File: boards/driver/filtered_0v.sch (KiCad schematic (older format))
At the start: 3 parts

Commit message: Driver board: a bit more schematic work and some initial footprint selections
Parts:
- R228: footprint Resistor_SMD:R_1206_3216Metric -> Resistor_SMD:R_0603_1608Metric
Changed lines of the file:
@@
 F 0 "R229" V 4395 3600 50  0000 C CNN
 F 1 "3k" V 4486 3600 50  0000 C CNN
-F 2 "Resistor_SMD:R_1206_3216Metric" V 4640 3590 50  0001 C CNN
+F 2 "Resistor_SMD:R_0603_1608Metric" V 4640 3590 50  0001 C CNN
 F 3 "~" H 4600 3600 50  0001 C CNN
 	1    4600 3600

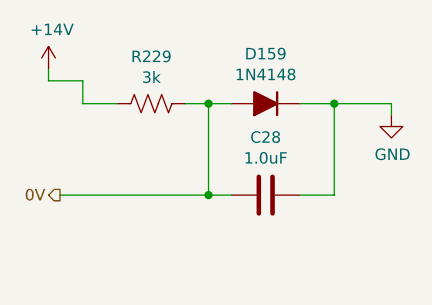
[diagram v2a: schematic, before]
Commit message: Driver board: fleshed out the hotswap controller, tweaked some resistors, and added some bypass caps
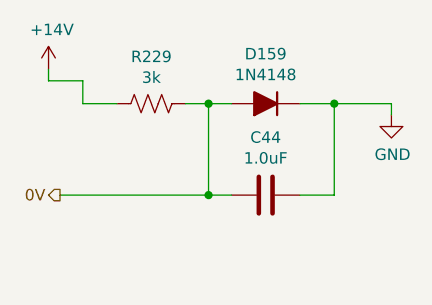
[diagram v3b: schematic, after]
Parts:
- renumbered C27 to C43
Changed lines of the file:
@@
 $EndDescr
 $Comp
-L lachesis:+14V #PWR0102
+L lachesis:+14V #PWR0105
 U 1 1 62980B09
 P 4150 3450
-AR Path="/6183FAE6/62980982/62980B09" Ref="#PWR0102"  Part="1"
-AR Path="/6183FAE6/6299B990/62980B09" Ref="#PWR0104"  Part="1"
-F 0 "#PWR0104" H 4150 3300 50  0001 C CNN
+AR Path="/6183FAE6/62980982/62980B09" Ref="#PWR0105"  Part="1"
+AR Path="/6183FAE6/6299B990/62980B09" Ref="#PWR0107"  Part="1"
+F 0 "#PWR0107" H 4150 3300 50  0001 C CNN
 F 1 "+14V" H 4165 3623 50  0000 C CNN
 F 2 "" H 4150 3450 50  0001 C CNN
@@
 0V
 $Comp
-L Device:C C27
+L Device:C C43
 U 1 1 62982B83
 P 5100 4000
-AR Path="/6183FAE6/62980982/62982B83" Ref="C27"  Part="1"
-AR Path="/6183FAE6/6299B990/62982B83" Ref="C28"  Part="1"
-F 0 "C28" V 4848 4000 50  0000 C CNN
+AR Path="/6183FAE6/62980982/62982B83" Ref="C43"  Part="1"
+AR Path="/6183FAE6/6299B990/62982B83" Ref="C44"  Part="1"
+F 0 "C44" V 4848 4000 50  0000 C CNN
 F 1 "1.0uF" V 4939 4000 50  0000 C CNN
 F 2 "" H 5138 3850 50  0001 C CNN
@@
 Connection ~ 5400 3600
 $Comp
-L power:GND #PWR0103
+L power:GND #PWR0106
 U 1 1 629836D4
 P 5650 3650
-AR Path="/6183FAE6/62980982/629836D4" Ref="#PWR0103"  Part="1"
-AR Path="/6183FAE6/6299B990/629836D4" Ref="#PWR0105"  Part="1"
-F 0 "#PWR0105" H 5650 3400 50  0001 C CNN
+AR Path="/6183FAE6/62980982/629836D4" Ref="#PWR0106"  Part="1"
+AR Path="/6183FAE6/6299B990/629836D4" Ref="#PWR0108"  Part="1"
+F 0 "#PWR0108" H 5650 3400 50  0001 C CNN
 F 1 "GND" H 5655 3477 50  0000 C CNN
 F 2 "" H 5650 3650 50  0001 C CNN

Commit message: Driver board: significant cleanup. Moved sense amp pairs into a subsheet, split tuning resistors into two globally, pushed input circuits into their corresponding sheets.
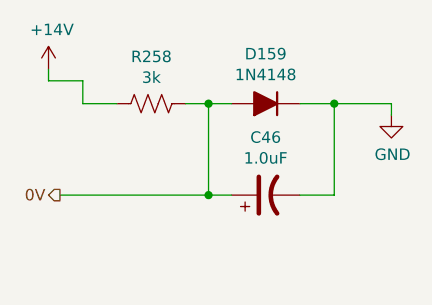
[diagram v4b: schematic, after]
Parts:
- removed C43: 1.0uF, symbol Device:C
- added C46: 1.0uF, Capacitor_Tantalum_SMD:CP_EIA-3216-18_Kemet-A, symbol Device:CP1
- renumbered R228 to R257
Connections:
- net 0V: now also C46.1
- net GND: now also C46.2
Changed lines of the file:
@@
 $Descr A4 11693 8268
 encoding utf-8
-Sheet 67 69
+Sheet 66 64
 Title ""
 Date ""
@@
 $EndDescr
 $Comp
-L lachesis:+14V #PWR0105
+L lachesis:+14V #PWR0122
 U 1 1 62980B09
 P 4150 3450
-AR Path="/6183FAE6/62980982/62980B09" Ref="#PWR0105"  Part="1"
-AR Path="/6183FAE6/6299B990/62980B09" Ref="#PWR0107"  Part="1"
-F 0 "#PWR0107" H 4150 3300 50  0001 C CNN
+AR Path="/6183FAE6/62980982/62980B09" Ref="#PWR0122"  Part="1"
+AR Path="/6183FAE6/6299B990/62980B09" Ref="#PWR0124"  Part="1"
+F 0 "#PWR0124" H 4150 3300 50  0001 C CNN
 F 1 "+14V" H 4165 3623 50  0000 C CNN
 F 2 "" H 4150 3450 50  0001 C CNN
@@
 $EndComp
 $Comp
-L Device:R_US R228
+L Device:R_US R257
 U 1 1 62981703
 P 4600 3600
-AR Path="/6183FAE6/62980982/62981703" Ref="R228"  Part="1"
-AR Path="/6183FAE6/6299B990/62981703" Ref="R229"  Part="1"
-F 0 "R229" V 4395 3600 50  0000 C CNN
+AR Path="/6183FAE6/62980982/62981703" Ref="R257"  Part="1"
+AR Path="/6183FAE6/6299B990/62981703" Ref="R258"  Part="1"
+F 0 "R258" V 4395 3600 50  0000 C CNN
 F 1 "3k" V 4486 3600 50  0000 C CNN
 F 2 "Resistor_SMD:R_0603_1608Metric" V 4640 3590 50  0001 C CNN
@@
 Text HLabel 4200 4000 0    50   Output ~ 0
 0V
-$Comp
-L Device:C C43
-U 1 1 62982B83
-P 5100 4000
-AR Path="/6183FAE6/62980982/62982B83" Ref="C43"  Part="1"
-AR Path="/6183FAE6/6299B990/62982B83" Ref="C44"  Part="1"
-F 0 "C44" V 4848 4000 50  0000 C CNN
-F 1 "1.0uF" V 4939 4000 50  0000 C CNN
-F 2 "" H 5138 3850 50  0001 C CNN
-F 3 "~" H 5100 4000 50  0001 C CNN
-	1    5100 4000
-	0    1    1    0
-$EndComp
 Wire Wire Line
 	4850 4000 4950 4000
@@
 Connection ~ 5400 3600
 $Comp
-L power:GND #PWR0106
+L power:GND #PWR0123
 U 1 1 629836D4
 P 5650 3650
-AR Path="/6183FAE6/62980982/629836D4" Ref="#PWR0106"  Part="1"
-AR Path="/6183FAE6/6299B990/629836D4" Ref="#PWR0108"  Part="1"
-F 0 "#PWR0108" H 5650 3400 50  0001 C CNN
+AR Path="/6183FAE6/62980982/629836D4" Ref="#PWR0123"  Part="1"
+AR Path="/6183FAE6/6299B990/629836D4" Ref="#PWR0125"  Part="1"
+F 0 "#PWR0125" H 5650 3400 50  0001 C CNN
 F 1 "GND" H 5655 3477 50  0000 C CNN
 F 2 "" H 5650 3650 50  0001 C CNN
@@
 	1    0    0    -1
 $EndComp
+$Comp
+L Device:CP1 C46
+U 1 1 628500B5
+P 5100 4000
+AR Path="/6183FAE6/6299B990/628500B5" Ref="C46"  Part="1"
+AR Path="/6183FAE6/62980982/628500B5" Ref="C45"  Part="1"
+F 0 "C46" V 5352 4000 50  0000 C CNN
+F 1 "1.0uF" V 5261 4000 50  0000 C CNN
+F 2 "Capacitor_Tantalum_SMD:CP_EIA-3216-18_Kemet-A" H 5100 4000 50  0001 C CNN
+F 3 "~" H 5100 4000 50  0001 C CNN
+	1    5100 4000
+	0    -1   -1   0
+$EndComp
 $EndSCHEMATC

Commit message: Driver board: integrated DIN 41612 backplane connector, and made a dedicated parity inhibit sheet with a different set resistor value.
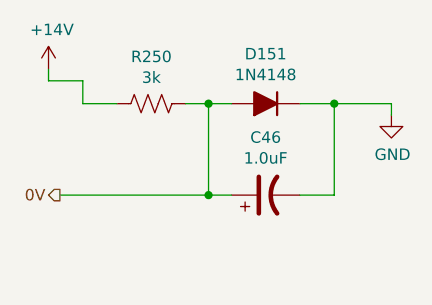
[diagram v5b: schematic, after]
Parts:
- renumbered D158 to D150, R257 to R249
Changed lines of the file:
@@
 $EndDescr
 $Comp
-L lachesis:+14V #PWR0122
+L lachesis:+14V #PWR0121
 U 1 1 62980B09
 P 4150 3450
-AR Path="/6183FAE6/62980982/62980B09" Ref="#PWR0122"  Part="1"
-AR Path="/6183FAE6/6299B990/62980B09" Ref="#PWR0124"  Part="1"
-F 0 "#PWR0124" H 4150 3300 50  0001 C CNN
+AR Path="/6183FAE6/62980982/62980B09" Ref="#PWR0121"  Part="1"
+AR Path="/6183FAE6/6299B990/62980B09" Ref="#PWR0123"  Part="1"
+F 0 "#PWR0123" H 4150 3300 50  0001 C CNN
 F 1 "+14V" H 4165 3623 50  0000 C CNN
 F 2 "" H 4150 3450 50  0001 C CNN
@@
 $EndComp
 $Comp
-L Device:R_US R257
+L Device:R_US R249
 U 1 1 62981703
 P 4600 3600
-AR Path="/6183FAE6/62980982/62981703" Ref="R257"  Part="1"
-AR Path="/6183FAE6/6299B990/62981703" Ref="R258"  Part="1"
-F 0 "R258" V 4395 3600 50  0000 C CNN
+AR Path="/6183FAE6/62980982/62981703" Ref="R249"  Part="1"
+AR Path="/6183FAE6/6299B990/62981703" Ref="R250"  Part="1"
+F 0 "R250" V 4395 3600 50  0000 C CNN
 F 1 "3k" V 4486 3600 50  0000 C CNN
 F 2 "Resistor_SMD:R_0603_1608Metric" V 4640 3590 50  0001 C CNN
@@
 	4300 3600 4450 3600
 $Comp
-L Device:D_ALT D158
+L Device:D_ALT D150
 U 1 1 629820FD
 P 5100 3600
-AR Path="/6183FAE6/62980982/629820FD" Ref="D158"  Part="1"
-AR Path="/6183FAE6/6299B990/629820FD" Ref="D159"  Part="1"
-F 0 "D159" H 5100 3383 50  0000 C CNN
+AR Path="/6183FAE6/62980982/629820FD" Ref="D150"  Part="1"
+AR Path="/6183FAE6/6299B990/629820FD" Ref="D151"  Part="1"
+F 0 "D151" H 5100 3383 50  0000 C CNN
 F 1 "1N4148" H 5100 3474 50  0000 C CNN
 F 2 "Diode_SMD:D_SOD-323" H 5100 3600 50  0001 C CNN
@@
 Connection ~ 5400 3600
 $Comp
-L power:GND #PWR0123
+L power:GND #PWR0122
 U 1 1 629836D4
 P 5650 3650
-AR Path="/6183FAE6/62980982/629836D4" Ref="#PWR0123"  Part="1"
-AR Path="/6183FAE6/6299B990/629836D4" Ref="#PWR0125"  Part="1"
-F 0 "#PWR0125" H 5650 3400 50  0001 C CNN
+AR Path="/6183FAE6/62980982/629836D4" Ref="#PWR0122"  Part="1"
+AR Path="/6183FAE6/6299B990/629836D4" Ref="#PWR0124"  Part="1"
+F 0 "#PWR0124" H 5650 3400 50  0001 C CNN
 F 1 "GND" H 5655 3477 50  0000 C CNN
 F 2 "" H 5650 3650 50  0001 C CNN

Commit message: Driver board: largely fleshed out part selection
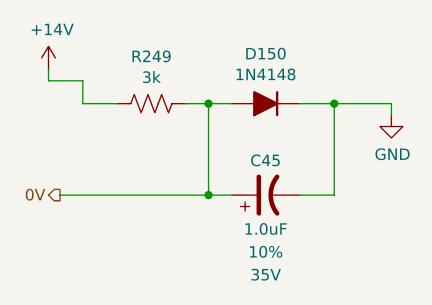
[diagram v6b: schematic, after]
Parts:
- C46: footprint Capacitor_Tantalum_SMD:CP_EIA-3216-18_Kemet-A -> Capacitor_Tantalum_SMD:CP_EIA-3528-21_Kemet-B; Digikey (none) -> https://www.digikey.com/en/products/detail/kemet/T495B105K0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; ESR (none) -> 1.5; Part Number (none) -> T495B105K035ATE1K5; Rating (none) -> 35V; Tolerance (none) -> 10%
- D150: Digikey (none) -> https://www.digikey.com/en/products/detail/smc-diode-soluti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; Part Number (none) -> 1N4148WSTR
- R249: Digikey (none) -> https://www.digikey.com/en/products/detail/vishay-dale/RCS0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; Part Number (none) -> RCS06033K00FKEA; Rating (none) -> 1/4W; Tolerance (none) -> 1%
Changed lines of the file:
@@
 $Descr A4 11693 8268
 encoding utf-8
-Sheet 66 64
+Sheet 59 64
 Title ""
 Date ""
@@
 AR Path="/6183FAE6/62980982/62981703" Ref="R249"  Part="1"
 AR Path="/6183FAE6/6299B990/62981703" Ref="R250"  Part="1"
-F 0 "R250" V 4395 3600 50  0000 C CNN
+F 0 "R249" V 4395 3600 50  0000 C CNN
 F 1 "3k" V 4486 3600 50  0000 C CNN
 F 2 "Resistor_SMD:R_0603_1608Metric" V 4640 3590 50  0001 C CNN
 F 3 "~" H 4600 3600 50  0001 C CNN
+F 4 "1%" V 4600 3600 50  0001 C CNN "Tolerance"
+F 5 "1/4W" V 4600 3600 50  0001 C CNN "Rating"
+F 6 "RCS06033K00FKEA" V 4600 3600 50  0001 C CNN "Part Number"
+F 7 "https://www.digikey.com/en/products/detail/vishay-dale/RCS06033K00FKEA/5868535" V 4600 3600 50  0001 C CNN "Digikey"
 	1    4600 3600
 	0    1    1    0
@@
 AR Path="/6183FAE6/62980982/629820FD" Ref="D150"  Part="1"
 AR Path="/6183FAE6/6299B990/629820FD" Ref="D151"  Part="1"
-F 0 "D151" H 5100 3383 50  0000 C CNN
+F 0 "D150" H 5100 3383 50  0000 C CNN
 F 1 "1N4148" H 5100 3474 50  0000 C CNN
 F 2 "Diode_SMD:D_SOD-323" H 5100 3600 50  0001 C CNN
 F 3 "~" H 5100 3600 50  0001 C CNN
+F 4 "https://www.digikey.com/en/products/detail/smc-diode-solutions/1N4148WSTR/6022449" H 5100 3600 50  0001 C CNN "Digikey"
+F 5 "1N4148WSTR" H 5100 3600 50  0001 C CNN "Part Number"
 	1    5100 3600
 	-1   0    0    1
@@
 AR Path="/6183FAE6/6299B990/628500B5" Ref="C46"  Part="1"
 AR Path="/6183FAE6/62980982/628500B5" Ref="C45"  Part="1"
-F 0 "C46" V 5352 4000 50  0000 C CNN
-F 1 "1.0uF" V 5261 4000 50  0000 C CNN
-F 2 "Capacitor_Tantalum_SMD:CP_EIA-3216-18_Kemet-A" H 5100 4000 50  0001 C CNN
+F 0 "C45" V 5250 4000 50  0000 C CNN
+F 1 "1.0uF" V 4950 4000 50  0000 C CNN
+F 2 "Capacitor_Tantalum_SMD:CP_EIA-3528-21_Kemet-B" H 5100 4000 50  0001 C CNN
 F 3 "~" H 5100 4000 50  0001 C CNN
+F 4 "10%" V 4850 4000 50  0000 C CNN "Tolerance"
+F 5 "35V" V 4750 4000 50  0000 C CNN "Rating"
+F 6 "1.5" V 5100 4000 50  0001 C CNN "ESR"
+F 7 "T495B105K035ATE1K5" V 5100 4000 50  0001 C CNN "Part Number"
+F 8 "https://www.digikey.com/en/products/detail/kemet/T495B105K035ATE1K5/9460136" V 5100 4000 50  0001 C CNN "Digikey"
 	1    5100 4000
 	0    -1   -1   0
